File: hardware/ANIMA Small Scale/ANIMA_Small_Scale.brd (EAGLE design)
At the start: 50 x 48.3 mm, 60 parts, among them J1 POW_CONNECTFEMALE-RA, Q1 MOSFET-PCHANNELSMD, Q2 MOSFET-PCHANNELSMD, Q3 MOSFET-PCHANNELSMD, U1 PIC32MX20F***B-44PIN, U12 MICRO-SDCARDSOCKET, U2 TPS54040, U3 MEDIATEK-3329, U5 MMA8451Q, U6 MAG3110

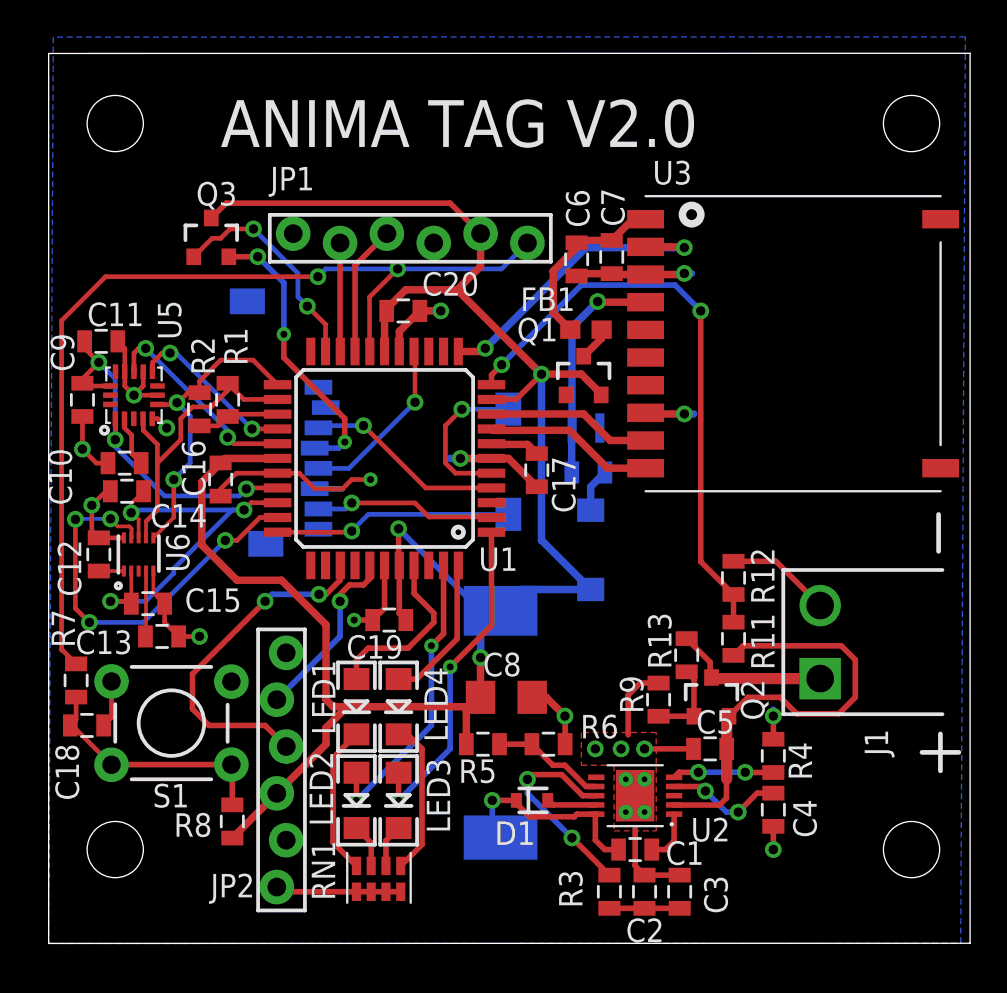
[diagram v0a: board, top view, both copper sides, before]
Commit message: board renovations complete attempting to diagnose I2C again
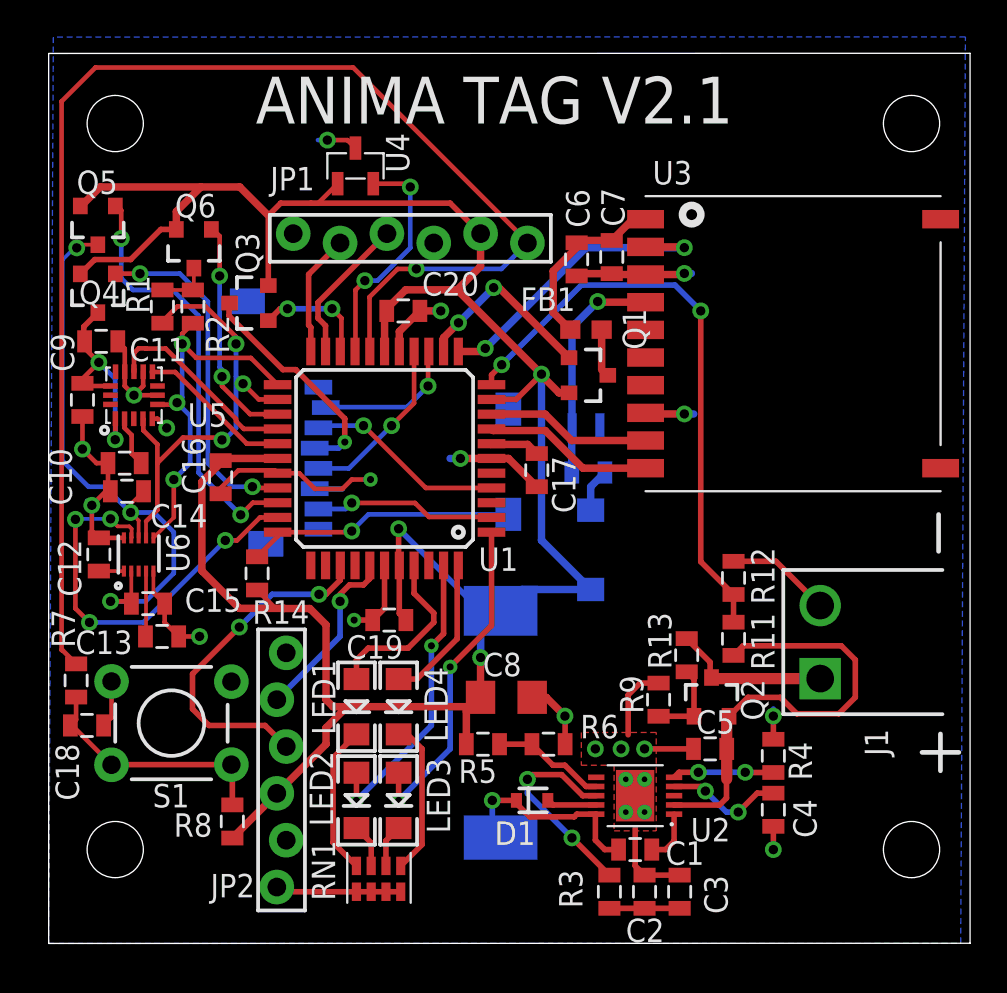
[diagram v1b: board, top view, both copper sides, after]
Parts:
- added Q4, Q5, Q6: MOSFET-PCHANNELSMD, ANIMAlib:SOT23-3
- added R14: 5.1K, ANIMAlib:0805
- added U4: TC1047, ANIMAlib:SOT-23B
- moved R1 6.17 mm to (6.17, 34.5), turned to 90 degrees
- moved R2 5.58 mm to (7.82, 34.5), turned to 90 degrees
- moved Q3 4.09 mm to (10.9, 34.7), turned to 90 degrees
- moved Q1 0.22 mm to (29.2, 30.8), turned to 270 degrees
- moved C16 0.13 mm to (9.32, 25.3)
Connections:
- new net ACCEL_POWER_EN: Q4.1, U1.30
- new net I2C_POWER_EN: Q6.1, U1.25
- new net MAG_POWER_EN: Q5.1, U1.31
- new net TEMPERATURE: U1.19, U4.P$2
- net ACCEL_POWER: now also Q4.3; no longer U1.30
- net CD1: now also R14.1
- net CD2: no longer U12.CD2
- net GND: now also U4.P$3
- net GPS_POWER: now also U1.13
- net I2C_POWER: now also Q6.3; no longer U1.25
- net MAG_POWER: now also Q5.3; no longer U1.31
- net MMA8451_INT1: now also U1.27; no longer U1.26
- net MMA8451_INT2: now also U1.26; no longer U1.27
- net N$22: now also Q3.3; no longer Q3.2
- net PGEC: now also U1.22; no longer U1.20
- net PGED: now also U1.21; no longer U1.19
- net SD_POWER_EN: now also U1.20; no longer U1.21
- net SS: now also U1.14
- net VCC3V3: now also Q3.2, Q4.2, Q5.2, Q6.2, R14.2, U4.P$1; no longer Q3.3
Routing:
- net VCC3V3: track 116.8 -> 141.0 mm
- net MAG_POWER_EN: track 0.00 -> 23.2 mm, vias 0 -> 2
- net MCLR: track 51.1 -> 73.7 mm, vias 2 -> 1
- net ACCEL_POWER_EN: track 0.00 -> 18.8 mm, vias 0 -> 2
- net TEMPERATURE: track 0.00 -> 12.6 mm, vias 0 -> 2
- net I2C_POWER_EN: track 0.00 -> 12.4 mm, vias 0 -> 2
- net GPS_POWER: track 0.00 -> 10.3 mm, vias 0 -> 2
- net MAG_POWER: track 23.6 -> 33.1 mm
- net CD2: track 8.68 -> 0.00 mm, vias 1 -> 0
- net SCL: track 16.6 -> 25.0 mm, vias 0 -> 3
- net ACCEL_POWER: track 20.9 -> 12.6 mm, vias 3 -> 2
- net SS: track 0.00 -> 8.00 mm, vias 0 -> 1
- net SD_POWER_EN: track 12.1 -> 6.39 mm
- net GND: track 91.8 -> 95.9 mm, vias 17 -> 18
- net SDA: track 17.0 -> 20.4 mm, vias 2 -> 3
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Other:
- board text added: "ANIMA TAG V2.1"
- board text removed: "ANIMA TAG V2.0"
